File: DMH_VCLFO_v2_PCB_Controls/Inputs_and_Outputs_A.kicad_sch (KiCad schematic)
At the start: 41 parts, among them J13 TS_Jack_6.35mm_Sw, J14 TS_Jack_6.35mm_Sw, J15 TS_Jack_6.35mm_Sw, J16 TS_Jack_6.35mm_Sw, J17 TS_Jack_6.35mm_Sw, J18 TS_Jack_6.35mm_Sw, J29 Conn_01x08, J30 Conn_01x08, J31 IDC_02x05, J32 Conn_01x08, J33 Conn_01x08, Q5 BC548, Q6 BC558, SW10 SPDT_OnOffOn, SW11 SW_SPDT, SW12 SW_SPDT, SW9 SW_SPDT, U3 TL074

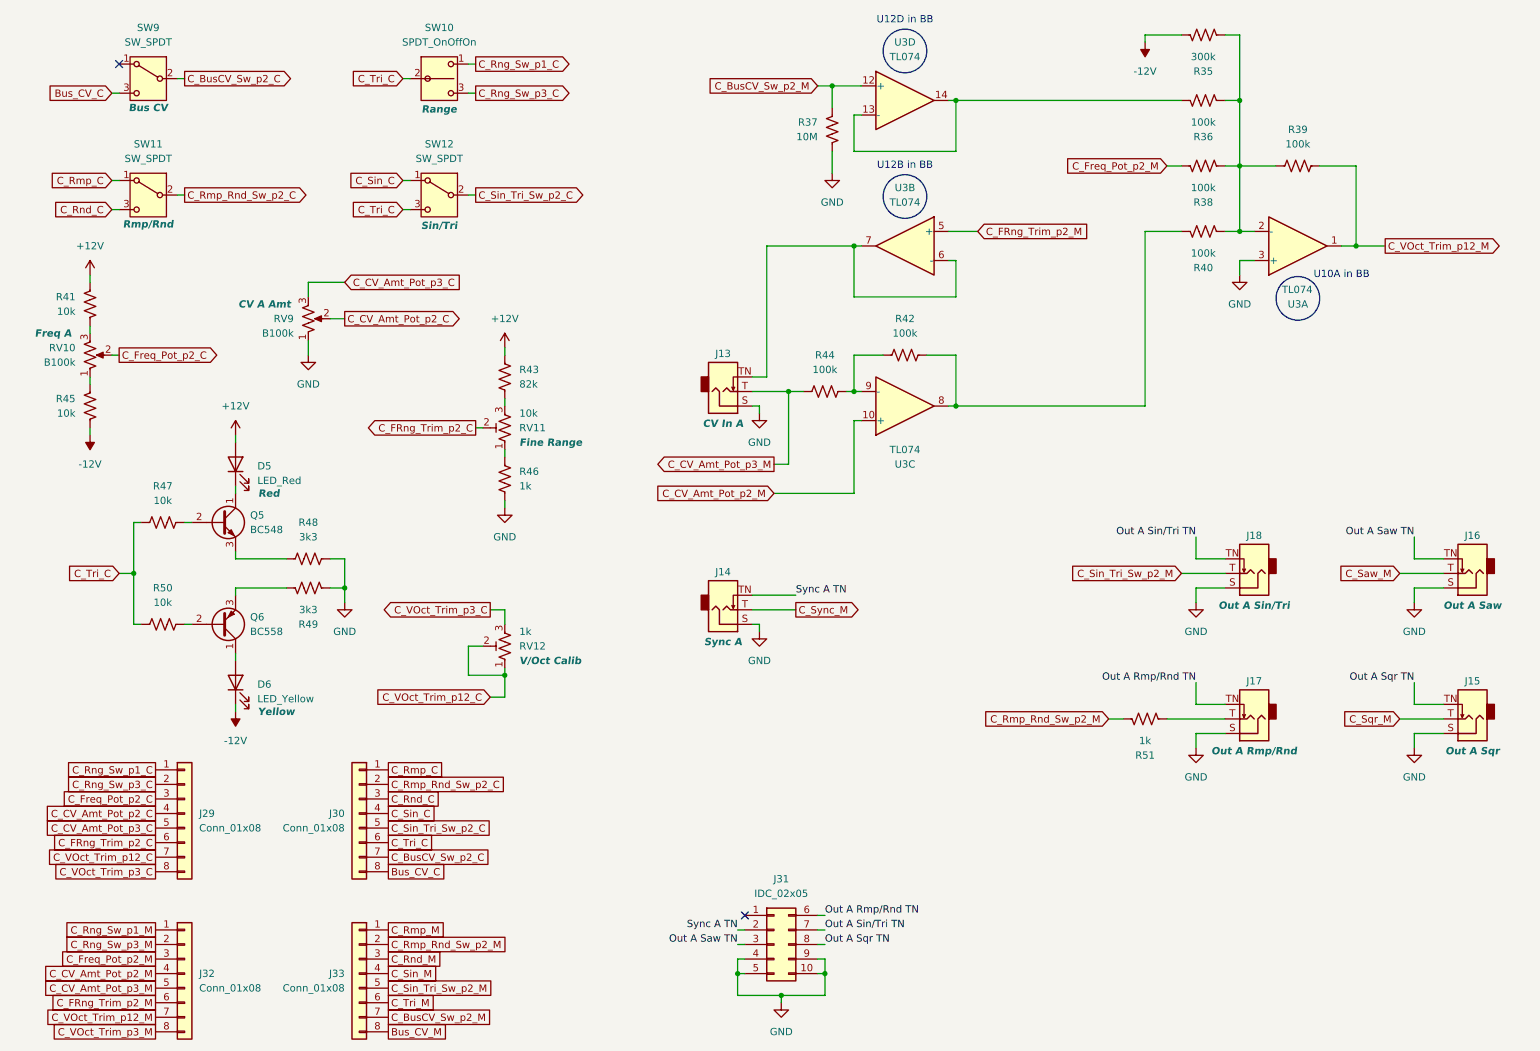
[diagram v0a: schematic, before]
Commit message: Controls PCB comp placement in progress
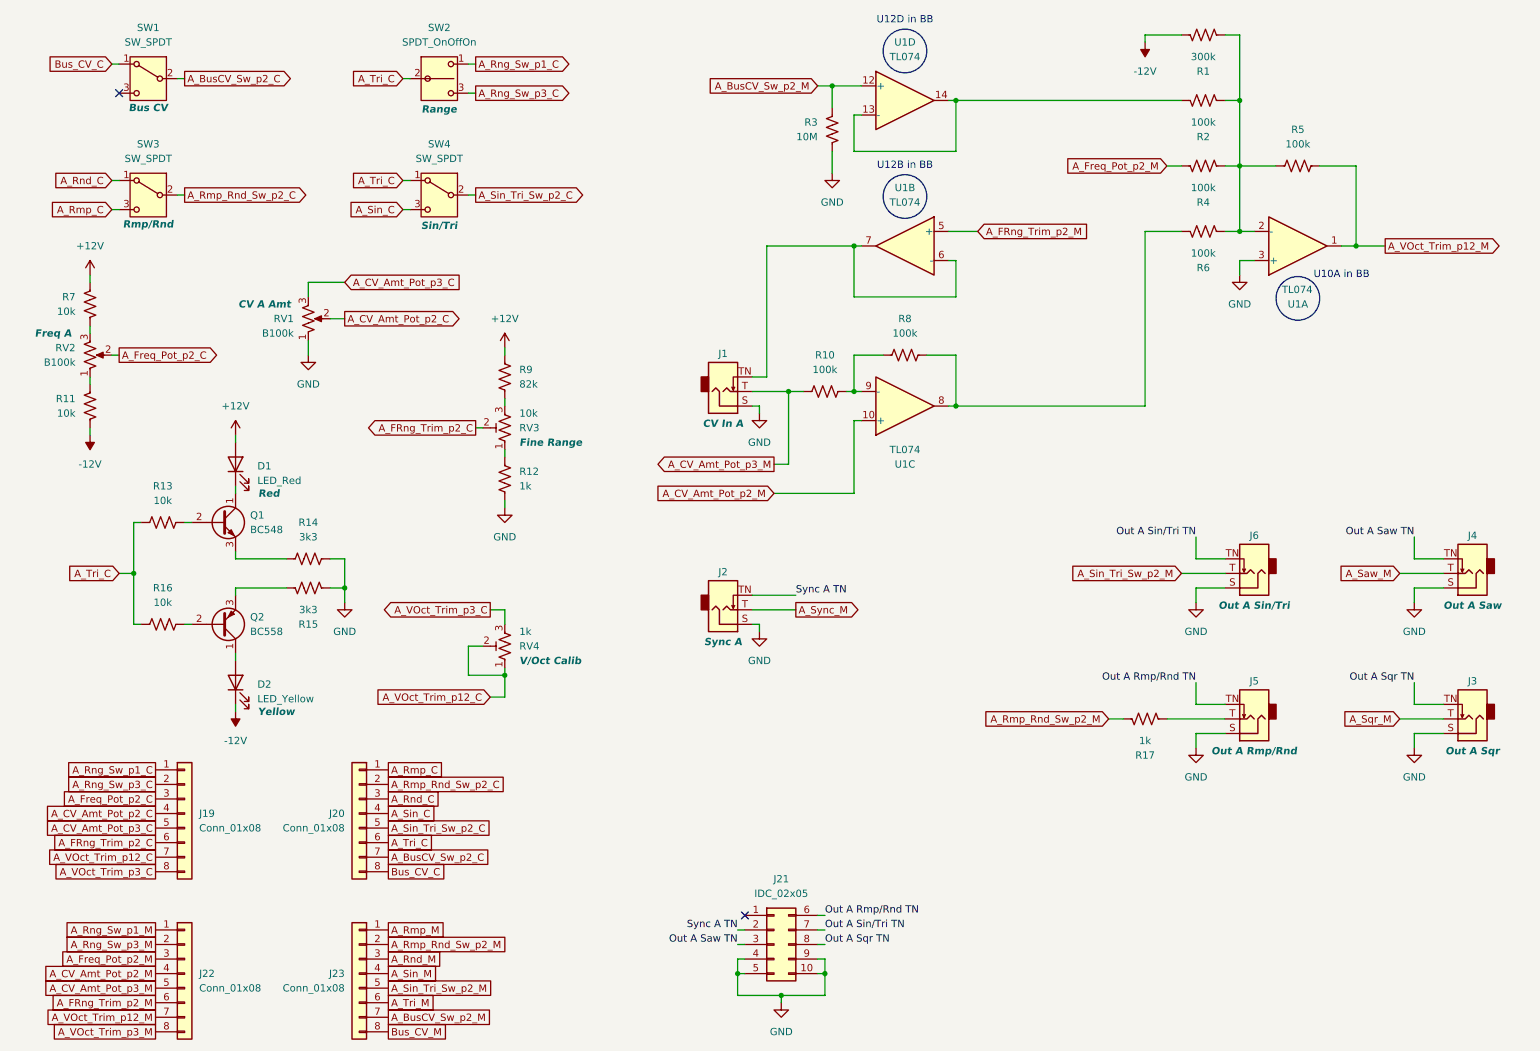
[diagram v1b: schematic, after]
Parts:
- J19: renamed from J29; footprint Connector_PinHeader_2.54mm:PinHeader_1x08_P2.54mm_Vertical -> Connector_PinSocket_2.54mm:PinSocket_1x08_P2.54mm_Vertical
- J20: renamed from J30; footprint Connector_PinHeader_2.54mm:PinHeader_1x08_P2.54mm_Vertical -> Connector_PinSocket_2.54mm:PinSocket_1x08_P2.54mm_Vertical
- renumbered D5 to D1, D6 to D2, J13 to J1, J14 to J2, J31 to J21, J32 to J22, J33 to J23, J15 to J3, J16 to J4, J17 to J5, J18 to J6, Q5 to Q1, Q6 to Q2, R35 to R1, R44 to R10, R45 to R11, R46 to R12, R47 to R13, R48 to R14, R49 to R15, R50 to R16, R51 to R17, R36 to R2, R37 to R3, R38 to R4, R39 to R5, R40 to R6, R41 to R7, R42 to R8, R43 to R9, RV9 to RV1, RV10 to RV2, RV11 to RV3, RV12 to RV4, SW9 to SW1, SW10 to SW2, SW11 to SW3, SW12 to SW4, U3 to U1
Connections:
- net Bus_CV_C: now also SW1.1 (A); no longer SW1.3 (C)
- net C_BusCV_Sw_p2_C renamed A_BusCV_Sw_p2_C
- net C_BusCV_Sw_p2_M renamed A_BusCV_Sw_p2_M
- net C_CV_Amt_Pot_p2_C renamed A_CV_Amt_Pot_p2_C
- net C_CV_Amt_Pot_p2_M renamed A_CV_Amt_Pot_p2_M
- net C_CV_Amt_Pot_p3_C renamed A_CV_Amt_Pot_p3_C
- net C_CV_Amt_Pot_p3_M renamed A_CV_Amt_Pot_p3_M
- net C_FRng_Trim_p2_C renamed A_FRng_Trim_p2_C
- net C_FRng_Trim_p2_M renamed A_FRng_Trim_p2_M
- net C_Freq_Pot_p2_C renamed A_Freq_Pot_p2_C
- net C_Freq_Pot_p2_M renamed A_Freq_Pot_p2_M
- net C_Rmp_C renamed A_Rmp_C
- net A_Rmp_C: now also SW3.3 (C); no longer SW3.1 (A)
- net C_Rmp_M renamed A_Rmp_M
- net C_Rmp_Rnd_Sw_p2_C renamed A_Rmp_Rnd_Sw_p2_C
- net C_Rmp_Rnd_Sw_p2_M renamed A_Rmp_Rnd_Sw_p2_M
- net C_Rnd_C renamed A_Rnd_C
- net A_Rnd_C: now also SW3.1 (A); no longer SW3.3 (C)
- net C_Rnd_M renamed A_Rnd_M
- net C_Rng_Sw_p1_C renamed A_Rng_Sw_p1_C
- net C_Rng_Sw_p1_M renamed A_Rng_Sw_p1_M
- net C_Rng_Sw_p3_C renamed A_Rng_Sw_p3_C
- net C_Rng_Sw_p3_M renamed A_Rng_Sw_p3_M
- net C_Saw_M renamed A_Saw_M
- net C_Sin_C renamed A_Sin_C
- net A_Sin_C: now also SW4.3 (C); no longer SW4.1 (A)
- net C_Sin_M renamed A_Sin_M
- net C_Sin_Tri_Sw_p2_C renamed A_Sin_Tri_Sw_p2_C
- net C_Sin_Tri_Sw_p2_M renamed A_Sin_Tri_Sw_p2_M
- net C_Sqr_M renamed A_Sqr_M
- net C_Sync_M renamed A_Sync_M
- net C_Tri_C renamed A_Tri_C
- net A_Tri_C: now also SW4.1 (A); no longer SW4.3 (C)
- net C_Tri_M renamed A_Tri_M
- net C_VOct_Trim_p12_C renamed A_VOct_Trim_p12_C
- net C_VOct_Trim_p12_M renamed A_VOct_Trim_p12_M
- net C_VOct_Trim_p3_C renamed A_VOct_Trim_p3_C
- net C_VOct_Trim_p3_M renamed A_VOct_Trim_p3_M

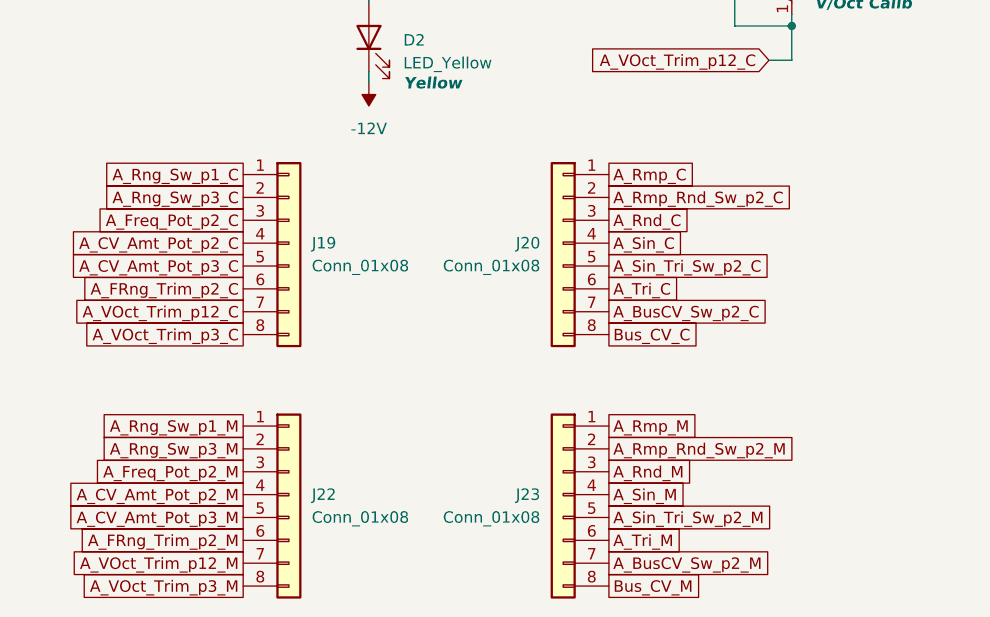
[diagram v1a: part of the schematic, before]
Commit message: Controls PCB routing done
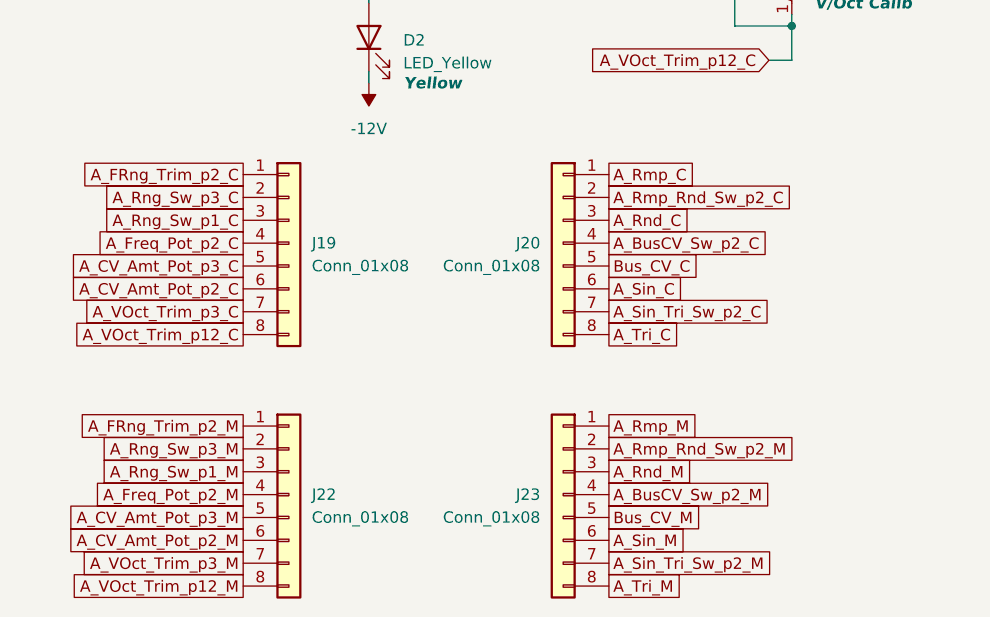
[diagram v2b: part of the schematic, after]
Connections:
- net A_BusCV_Sw_p2_C: now also J20.4 (Pin_4); no longer J20.7 (Pin_7)
- net A_BusCV_Sw_p2_M: now also J23.4 (Pin_4); no longer J23.7 (Pin_7)
- net A_CV_Amt_Pot_p2_C: now also J19.6 (Pin_6); no longer J19.4 (Pin_4)
- net A_CV_Amt_Pot_p2_M: now also J22.6 (Pin_6); no longer J22.4 (Pin_4)
- net A_FRng_Trim_p2_C: now also J19.1 (Pin_1); no longer J19.6 (Pin_6)
- net A_FRng_Trim_p2_M: now also J22.1 (Pin_1); no longer J22.6 (Pin_6)
- net A_Freq_Pot_p2_C: now also J19.4 (Pin_4); no longer J19.3 (Pin_3)
- net A_Freq_Pot_p2_M: now also J22.4 (Pin_4); no longer J22.3 (Pin_3)
- net A_Rng_Sw_p1_C: now also J19.3 (Pin_3); no longer J19.1 (Pin_1)
- net A_Rng_Sw_p1_M: now also J22.3 (Pin_3); no longer J22.1 (Pin_1)
- net A_Sin_C: now also J20.6 (Pin_6); no longer J20.4 (Pin_4)
- net A_Sin_M: now also J23.6 (Pin_6); no longer J23.4 (Pin_4)
- net A_Sin_Tri_Sw_p2_C: now also J20.7 (Pin_7); no longer J20.5 (Pin_5)
- net A_Sin_Tri_Sw_p2_M: now also J23.7 (Pin_7); no longer J23.5 (Pin_5)
- net A_Tri_C: now also J20.8 (Pin_8); no longer J20.6 (Pin_6)
- net A_Tri_M: now also J23.8 (Pin_8); no longer J23.6 (Pin_6)
- net A_VOct_Trim_p12_C: now also J19.8 (Pin_8); no longer J19.7 (Pin_7)
- net A_VOct_Trim_p12_M: now also J22.8 (Pin_8); no longer J22.7 (Pin_7)
- net A_VOct_Trim_p3_C: now also J19.7 (Pin_7); no longer J19.8 (Pin_8)
- net A_VOct_Trim_p3_M: now also J22.7 (Pin_7); no longer J22.8 (Pin_8)
- net Bus_CV_C: now also J20.5 (Pin_5); no longer J20.8 (Pin_8)
- net Bus_CV_M: now also J23.5 (Pin_5); no longer J23.8 (Pin_8)

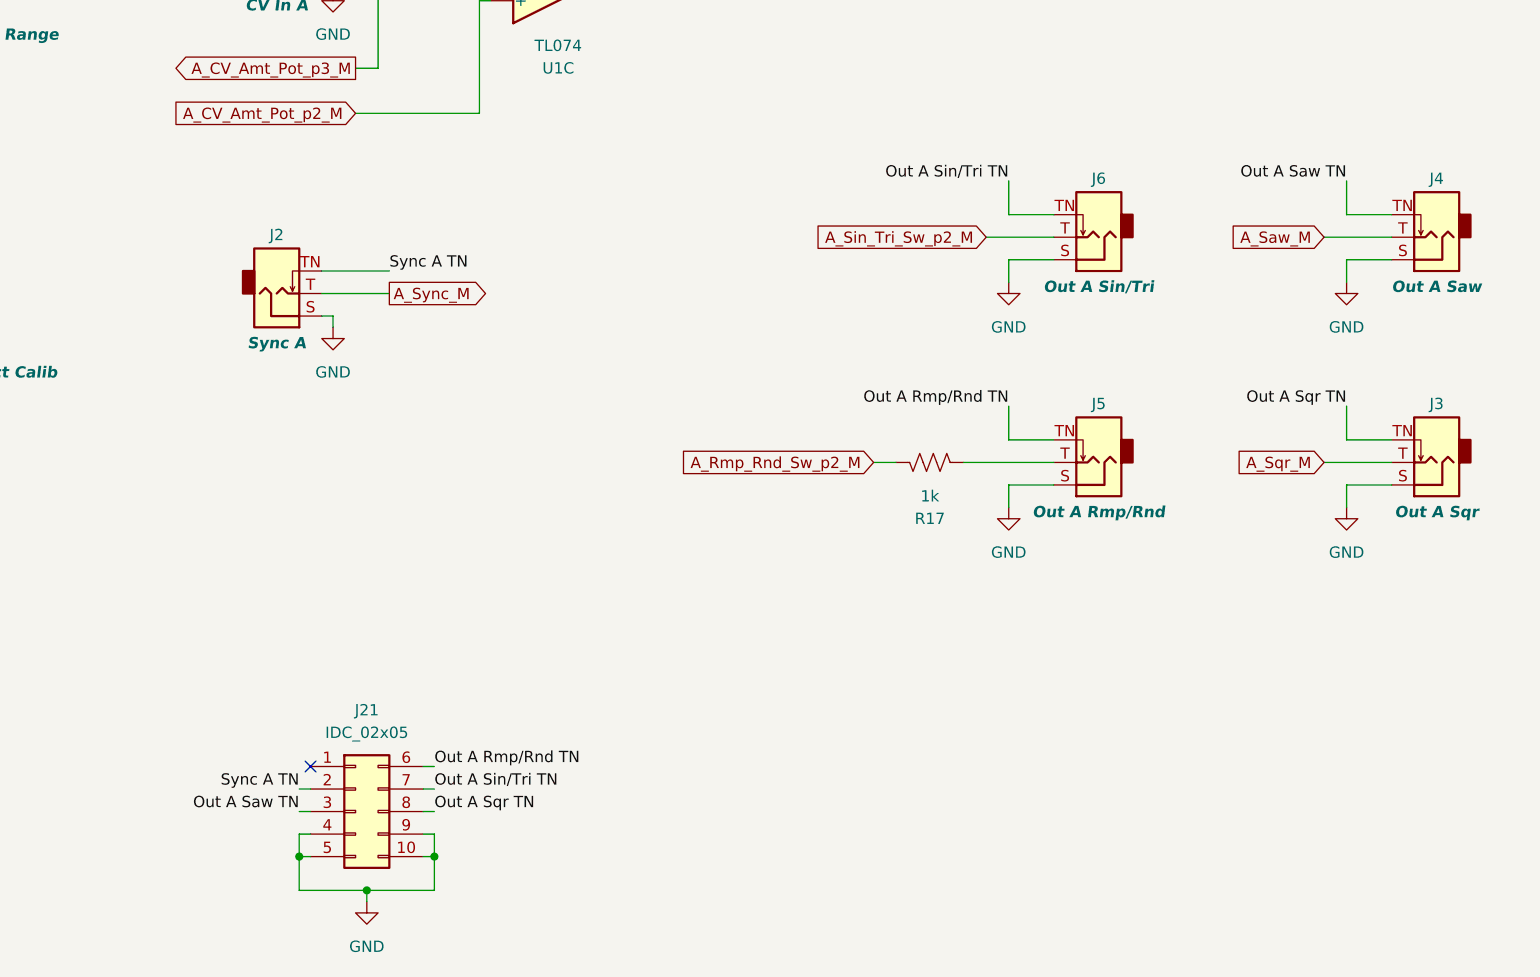
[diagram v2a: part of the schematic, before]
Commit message: Synced Controls PCB with Main
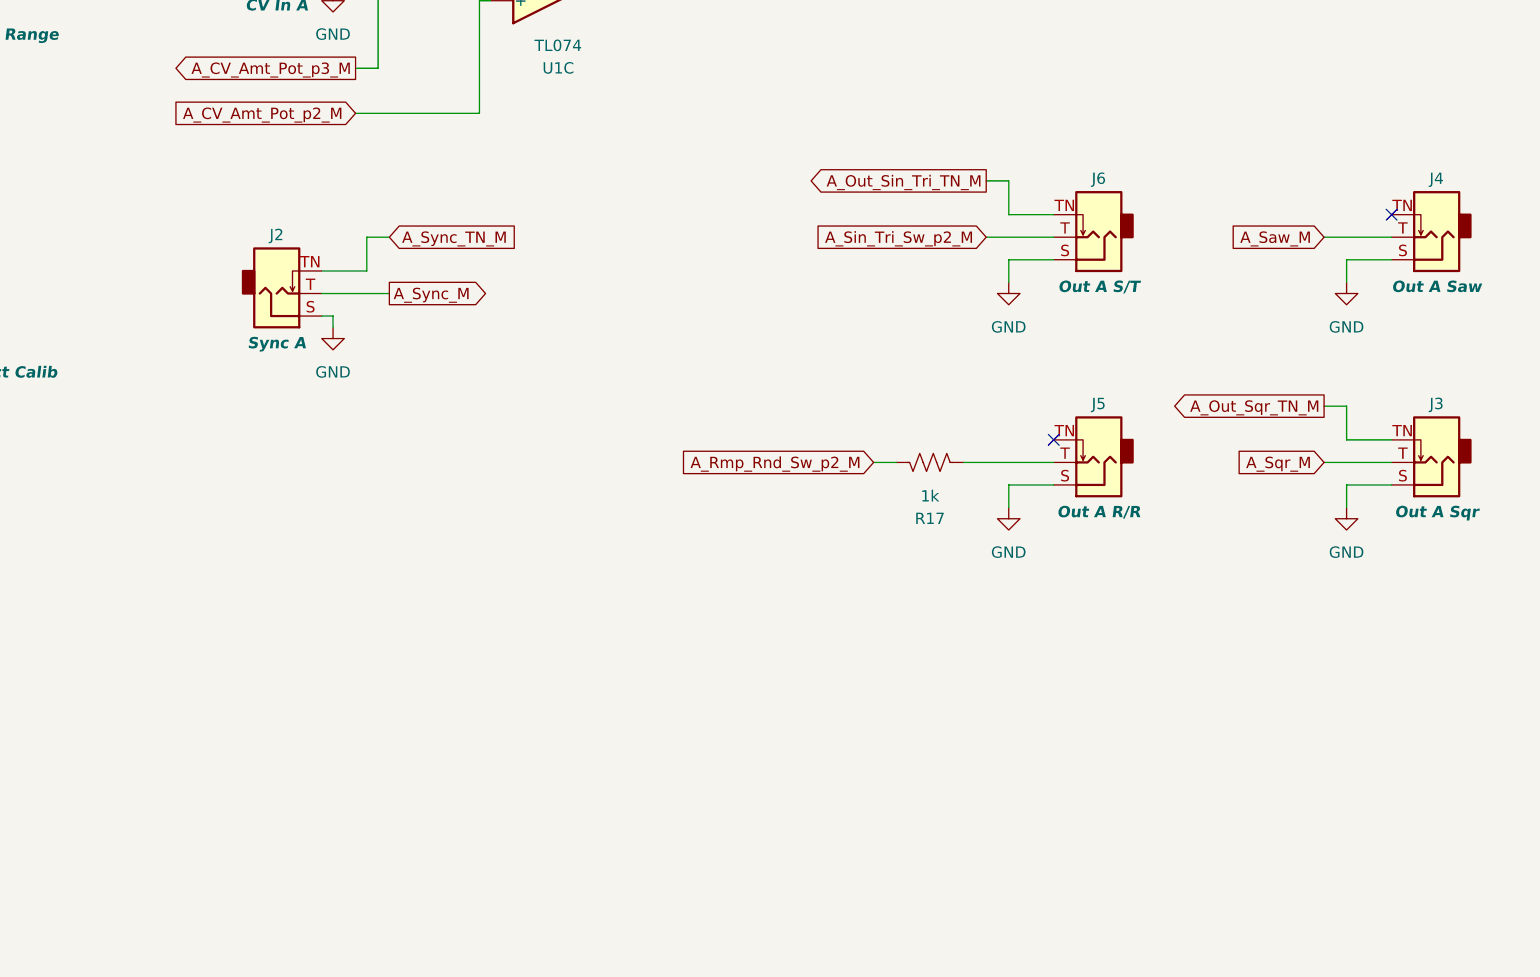
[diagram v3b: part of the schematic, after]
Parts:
- removed J21: IDC_02x05, SynthStuff:IDC-Header_2x05_P2.54mm_Vertical_BackBone, symbol SynthStuff:BackBone_Connector_10Pin
- J5: Function Out A Rmp/Rnd -> Out A R/R
- J6: Function Out A Sin/Tri -> Out A S/T
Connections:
- net Out A Rmp/Rnd TN: no longer names the net of J5.TN
- net Out A Saw TN: no longer names the net of J4.TN
- net Out A Sin/Tri TN renamed A_Out_Sin_Tri_TN_M
- net Out A Sqr TN renamed A_Out_Sqr_TN_M
- net Sync A TN renamed A_Sync_TN_M
- no-connect marks 2 -> 3
